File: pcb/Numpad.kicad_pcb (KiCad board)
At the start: 2 copper layers, 76.2 x 117.6 mm, 48 parts, among them P2 HOLE, P3 HOLE, P4 HOLE, P5 HOLE, P6 CONN_01X12, P7 CONN_01X12, SW1 F13, SW10 8, SW11 9, SW12 PLUS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

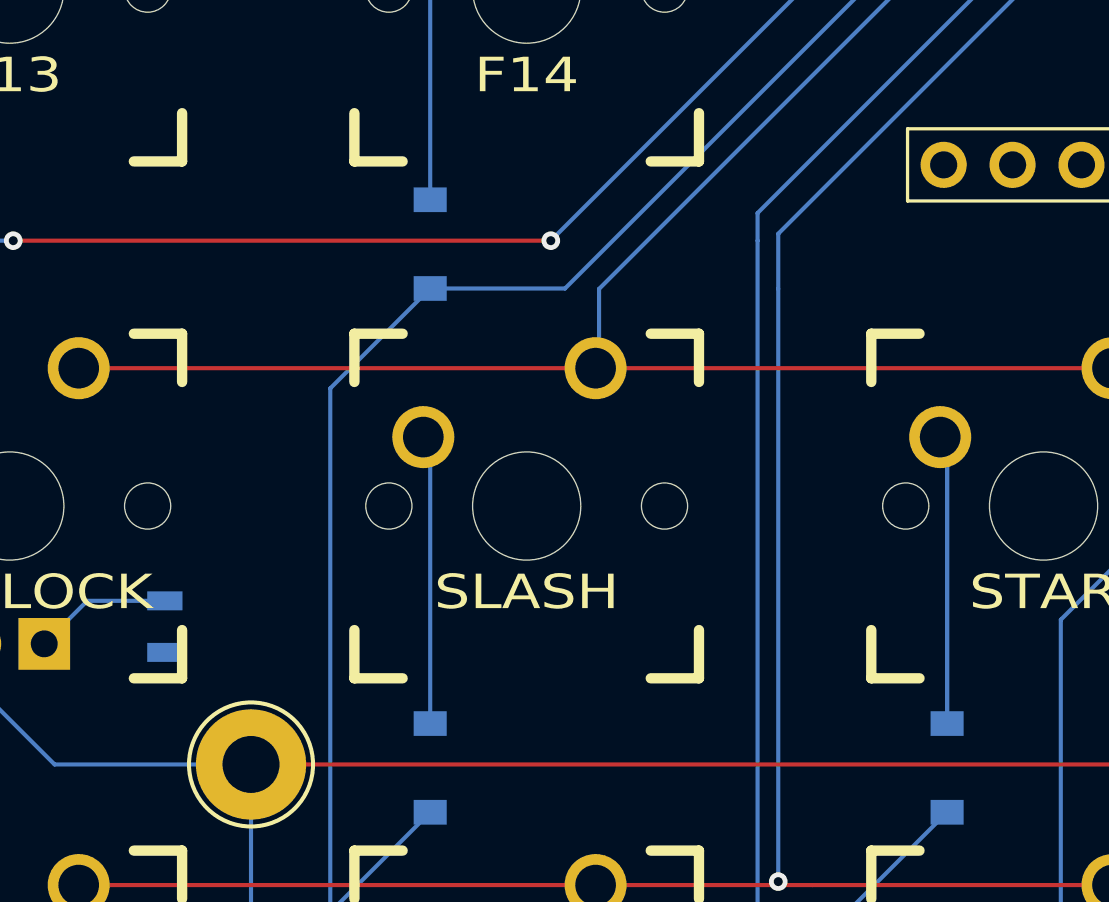
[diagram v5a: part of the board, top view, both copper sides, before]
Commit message: Wire up Numlock LED
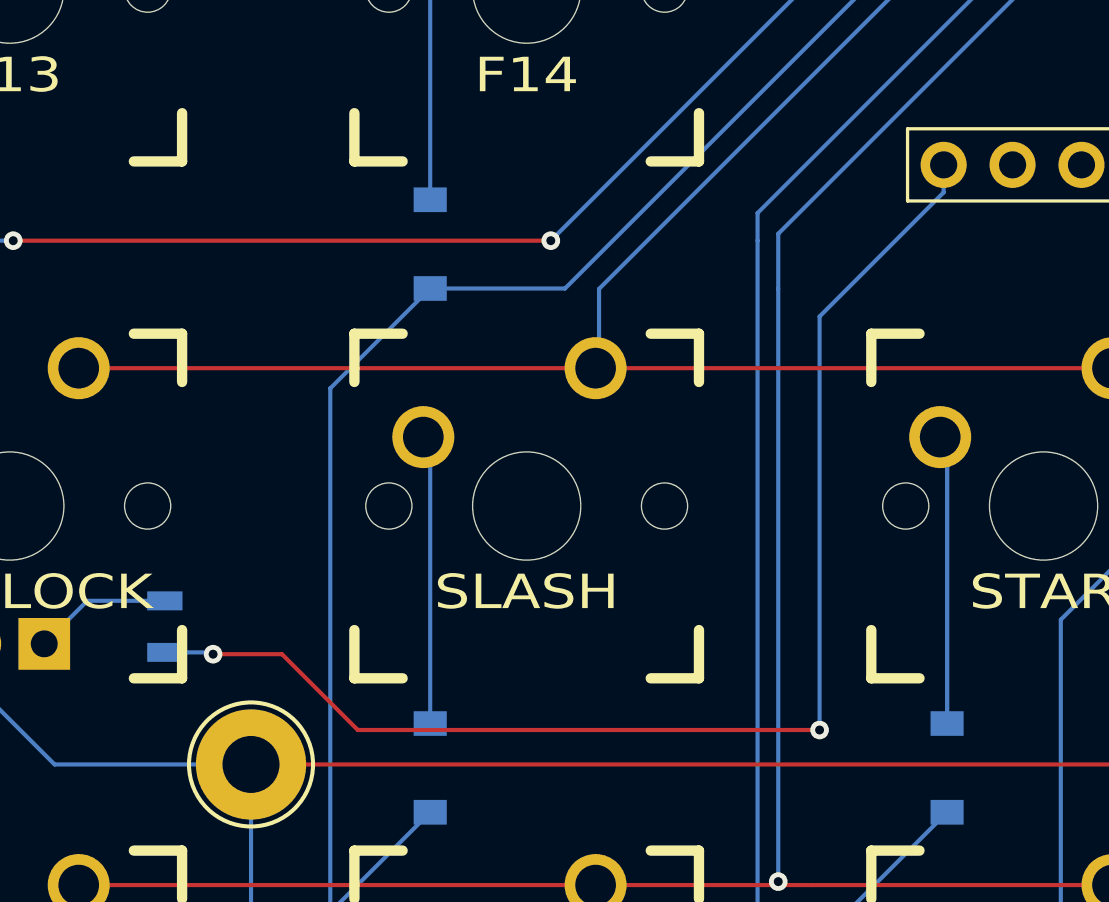
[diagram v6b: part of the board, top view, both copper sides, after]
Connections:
- P7 pad 12: Net-(P7-Pad12) -> /NUMLOCK_LED
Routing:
- net /NUMLOCK_LED: track 0.00 -> 48.0 mm, vias 0 -> 2
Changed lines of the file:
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@@
 (kicad_pcb (version 4) (host pcbnew 4.0.4-stable)
   (general
-    (links 68)
+    (links 69)
     (no_connects 0)
-    (area 65.963799 50.411666 142.316201 168.986201)
+    (area 65.989999 51.257999 142.290001 168.960001)
     (thickness 1.6)
     (drawings 13)
-    (tracks 225)
+    (tracks 235)
     (zones 0)
     (modules 48)
-    (nets 47)
+    (nets 46)
   )
   (page A4)
@@
   (net 44 "Net-(P7-Pad10)")
   (net 45 "Net-(P7-Pad11)")
-  (net 46 "Net-(P7-Pad12)")
   (net_class Default "This is the default net class."
     (clearance 0.1524)
@@
     (add_net "Net-(P7-Pad10)")
     (add_net "Net-(P7-Pad11)")
-    (add_net "Net-(P7-Pad12)")
     (add_net "Net-(P7-Pad4)")
     (add_net "Net-(P7-Pad9)")
@@
       (net 45 "Net-(P7-Pad11)"))
     (pad 12 thru_hole oval (at 0 27.94 270) (size 1.7 1.7) (drill 1) (layers *.Cu *.Mask)
-      (net 46 "Net-(P7-Pad12)"))
+      (net 28 /NUMLOCK_LED))
     (model ${KISYS3DMOD}/Pin_Headers.3dshapes/Pin_Header_Straight_1x12_Pitch2.54mm.wrl
       (at (xyz 0 -0.55 0))
@@
   (segment (start 76.835 88.265) (end 78.42 86.68) (width 0.1524) (layer B.Cu) (net 27))
   (segment (start 78.42 86.68) (end 81.28 86.68) (width 0.1524) (layer B.Cu) (net 27))
+  (segment (start 105.41 76.2) (end 109.982 71.628) (width 0.1524) (layer B.Cu) (net 28))
+  (segment (start 82.992 88.58) (end 83.058 88.646) (width 0.1524) (layer B.Cu) (net 28))
+  (via (at 83.058 88.646) (size 0.6858) (drill 0.3302) (layers F.Cu B.Cu) (net 28))
+  (segment (start 83.058 88.646) (end 85.598 88.646) (width 0.1524) (layer F.Cu) (net 28))
+  (segment (start 85.598 88.646) (end 88.392 91.44) (width 0.1524) (layer F.Cu) (net 28))
+  (segment (start 88.392 91.44) (end 105.41 91.44) (width 0.1524) (layer F.Cu) (net 28))
+  (via (at 105.41 91.44) (size 0.6858) (drill 0.3302) (layers F.Cu B.Cu) (net 28))
+  (segment (start 105.41 91.44) (end 105.41 76.2) (width 0.1524) (layer B.Cu) (net 28))
+  (segment (start 81.28 88.58) (end 82.992 88.58) (width 0.1524) (layer B.Cu) (net 28))
+  (segment (start 109.982 71.628) (end 109.982 70.612) (width 0.1524) (layer B.Cu) (net 28) (status 800000))
   (segment (start 136.652 73.406) (end 135.636 73.406) (width 0.1524) (layer F.Cu) (net 29))
   (via (at 140.716 73.406) (size 0.6858) (drill 0.3302) (layers F.Cu B.Cu) (net 29))

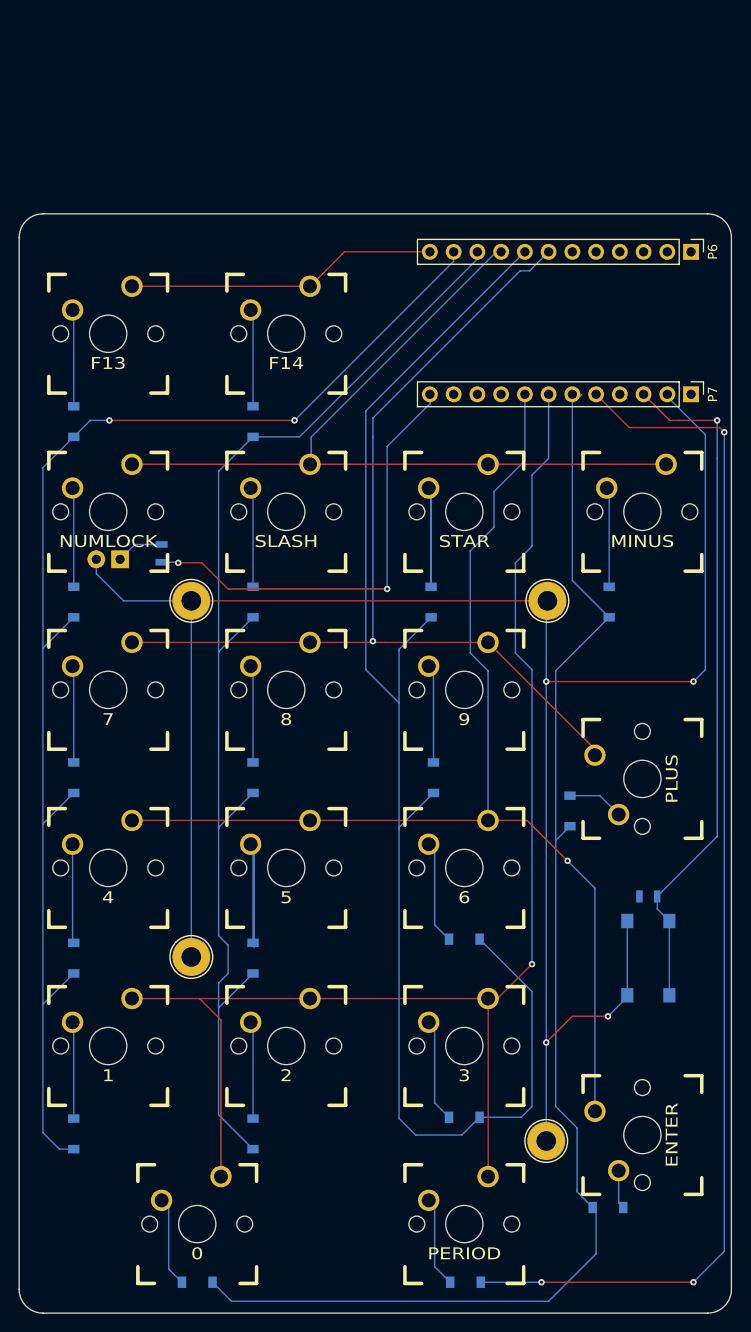
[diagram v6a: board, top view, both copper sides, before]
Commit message: Change wires to match prototype, add pullups for columns
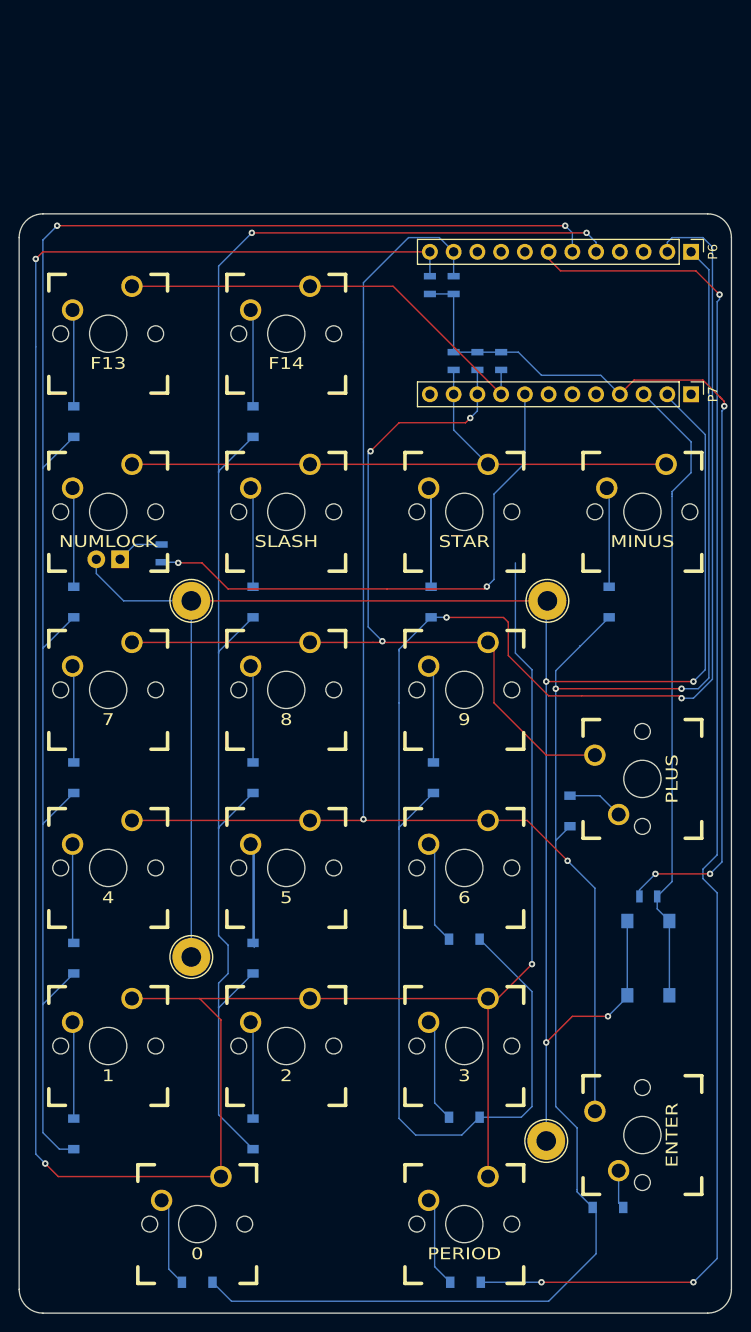
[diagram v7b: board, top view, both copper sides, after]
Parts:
- added R5: R, Keyboard:R_0805, B.Cu at (117.6, 67.1)
- added R6: R, Keyboard:R_0805, B.Cu at (112.5, 67.1)
- added R7: R, Keyboard:R_0805, B.Cu at (115.1, 67.1)
- added R8: R, Keyboard:R_0805, B.Cu at (112.5, 58.9)
- added R9: R, Keyboard:R_0805, B.Cu at (110.0, 58.9)
- R4: value 10k -> R
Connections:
- P6 pad 1: Net-(P6-Pad1) -> /COL3
- P6 pad 10: /COL1 -> Net-(P6-Pad10)
- P6 pad 11: /COL0 -> /ROW3
- P6 pad 12: /ROW0 -> /ROW4
- P6 pad 2: Net-(P6-Pad2) -> /COL2
- P6 pad 5: Net-(P6-Pad5) -> /COL1
- P6 pad 6: Net-(P6-Pad6) -> /COL0
- P6 pad 7: /ROW2 -> /COL4
- P6 pad 8: /COL2 -> Net-(P6-Pad8)
- P6 pad 9: /ROW1 -> Net-(P6-Pad9)
- P7 pad 10: Net-(P7-Pad10) -> /ROW2
- P7 pad 11: Net-(P7-Pad11) -> /ROW1
- P7 pad 12: /NUMLOCK_LED -> Net-(P7-Pad12)
- P7 pad 4: Net-(P7-Pad4) -> VCC
- P7 pad 5: /COL4 -> Net-(P7-Pad5)
- P7 pad 6: /COL3 -> Net-(P7-Pad6)
- P7 pad 7: /ROW4 -> Net-(P7-Pad7)
- P7 pad 8: /ROW3 -> /NUMLOCK_LED
- P7 pad 9: Net-(P7-Pad9) -> /ROW0
- R4 pad 2: +5V -> VCC
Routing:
- net /ROW4: track 146.5 -> 288.7 mm, vias 1 -> 3
- net VCC: track 0.00 -> 101.7 mm, vias 0 -> 3
- net /COL3: track 144.3 -> 181.7 mm, vias 0 -> 2
- net /COL0: track 143.6 -> 178.2 mm
- net /COL1: track 128.8 -> 161.5 mm, vias 0 -> 2
- net /COL2: track 153.6 -> 186.1 mm, vias 0 -> 2
- net /ROW3: track 125.2 -> 148.9 mm, vias 1 -> 2
- net /COL4: track 130.4 -> 151.5 mm
- net /ROW1: track 88.7 -> 69.0 mm
- net /ROW0: track 33.6 -> 47.1 mm
- net /NUMLOCK_LED: track 48.0 -> 58.3 mm
- net /ROW2: track 105.1 -> 96.6 mm, vias 1 -> 3
- net /ISP_RESET: track 73.7 -> 68.4 mm, vias 1 -> 0
- net Net-(P6-Pad10): track 0.00 -> 0.76 mm
- net Net-(P6-Pad9): track 0.00 -> 0.51 mm

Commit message: fix a track
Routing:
- net /ROW4: track 288.7 -> 239.8 mm, vias 3 -> 2
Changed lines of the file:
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@@
     (links 80)
     (no_connects 0)
-    (area 65.989999 51.257999 142.290001 168.960001)
+    (area 65.938399 50.386266 142.341601 169.011601)
     (thickness 1.6)
     (drawings 13)
-    (tracks 311)
+    (tracks 306)
     (zones 0)
     (modules 53)
@@
   (segment (start 103.886 97.155) (end 105.156 97.155) (width 0.1524) (layer F.Cu) (net 31))
   (segment (start 105.156 97.155) (end 116.205 97.155) (width 0.1524) (layer F.Cu) (net 31))
-  (segment (start 112.522 55.372) (end 112.522 57.978) (width 0.1524) (layer B.Cu) (net 32) (status C00000))
+  (segment (start 112.522 55.372) (end 112.522 57.978) (width 0.1524) (layer B.Cu) (net 32))
   (segment (start 112.522 55.372) (end 110.998 53.848) (width 0.1524) (layer B.Cu) (net 32))
   (segment (start 102.87 58.674) (end 102.87 65.024) (width 0.1524) (layer B.Cu) (net 32))
@@
   (segment (start 97.155 116.205) (end 102.87 116.205) (width 0.1524) (layer F.Cu) (net 32))
   (segment (start 102.87 116.205) (end 116.205 116.205) (width 0.1524) (layer F.Cu) (net 32))
-  (segment (start 109.982 55.372) (end 109.982 57.978) (width 0.1524) (layer B.Cu) (net 33) (status C00000))
+  (segment (start 109.982 55.372) (end 109.982 57.978) (width 0.1524) (layer B.Cu) (net 33))
   (segment (start 109.982 55.372) (end 68.58 55.372) (width 0.1524) (layer F.Cu) (net 33))
   (segment (start 70.231 154.305) (end 87.63 154.305) (width 0.1524) (layer F.Cu) (net 33))
@@
   (segment (start 68.58 55.372) (end 67.818 56.134) (width 0.1524) (layer F.Cu) (net 33))
   (segment (start 116.205 135.255) (end 117.221 135.255) (width 0.1524) (layer F.Cu) (net 33))
-  (segment (start 117.221 135.255) (end 120.904 131.572) (width 0.1524) (layer F.Cu) (net 33))
-  (via (at 120.904 131.572) (size 0.6858) (drill 0.3302) (layers F.Cu B.Cu) (net 33))
   (segment (start 116.205 135.255) (end 116.205 154.305) (width 0.1524) (layer F.Cu) (net 33))
   (segment (start 85.344 135.255) (end 87.63 137.541) (width 0.1524) (layer F.Cu) (net 33))
@@
   (segment (start 85.344 135.255) (end 97.155 135.255) (width 0.1524) (layer F.Cu) (net 33))
   (segment (start 97.155 135.255) (end 116.205 135.255) (width 0.1524) (layer F.Cu) (net 33))
-  (segment (start 120.904 131.572) (end 120.904 100.076) (width 0.1524) (layer B.Cu) (net 33))
-  (segment (start 120.904 100.076) (end 119.126 98.298) (width 0.1524) (layer B.Cu) (net 33))
-  (segment (start 119.126 98.298) (end 119.126 88.646) (width 0.1524) (layer B.Cu) (net 33))
   (segment (start 117.602 55.372) (end 117.094 55.372) (width 0.1524) (layer B.Cu) (net 38))
   (segment (start 115.062 55.372) (end 115.062 56.134) (width 0.1524) (layer B.Cu) (net 39))
-  (segment (start 112.522 59.878) (end 112.522 66.106) (width 0.1524) (layer B.Cu) (net 44) (status C00000))
-  (segment (start 109.982 59.878) (end 112.522 59.878) (width 0.1524) (layer B.Cu) (net 44) (status C00000))
+  (segment (start 112.522 59.878) (end 112.522 66.106) (width 0.1524) (layer B.Cu) (net 44))
+  (segment (start 109.982 59.878) (end 112.522 59.878) (width 0.1524) (layer B.Cu) (net 44))
   (segment (start 115.062 66.106) (end 117.602 66.106) (width 0.1524) (layer B.Cu) (net 44))
   (segment (start 112.522 66.106) (end 115.062 66.106) (width 0.1524) (layer B.Cu) (net 44))
